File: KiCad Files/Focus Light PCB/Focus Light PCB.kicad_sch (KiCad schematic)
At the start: 1 part, among them SW1 TS1603-TZ38HBM

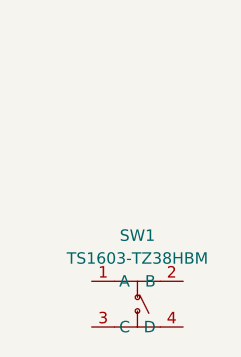
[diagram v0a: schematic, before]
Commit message: Small progress on kicad file due to switching over to easyeda
(KiCad folder will be deleted soon)
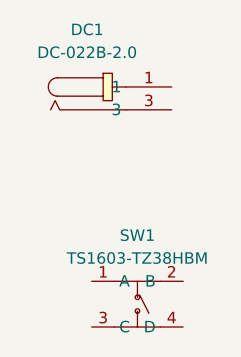
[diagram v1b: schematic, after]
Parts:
- added DC1: DC-022B-2.0, EasyEDA:DC-IN-TH_DC-022B-2.0, symbol EasyEDA:DC-022B-2.0
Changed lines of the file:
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@@
+		)
+	)
+	(symbol
+		(lib_id "EasyEDA:DC-022B-2.0")
+		(at 125.73 97.79 0)
+		(unit 1)
+		(body_style 1)
+		(exclude_from_sim no)
+		(in_bom yes)
+		(on_board yes)
+		(in_pos_files yes)
+		(dnp no)
+		(fields_autoplaced yes)
+		(property "Reference" "DC1"
+			(at 122.6822 91.44 0)
+			(show_name no)
+			(do_not_autoplace no)
+			(effects
+				(font
+					(size 1.27 1.27)
+				)
+			)
+		)
+		(property "Value" "DC-022B-2.0"
+			(at 122.6822 93.98 0)
+			(show_name no)
+			(do_not_autoplace no)
+			(effects
+				(font
+					(size 1.27 1.27)
+				)
+			)
+		)
+		(property "Footprint" "EasyEDA:DC-IN-TH_DC-022B-2.0"
+			(at 125.73 107.95 0)
+			(hide yes)
+			(show_name no)
+			(do_not_autoplace no)
+			(effects
+				(font
+					(size 1.27 1.27)
+				)
+			)
+		)
+		(property "Datasheet" "https://lcsc.com/product-detail/Power-Connectors_XKB-Enterprise-DC-022B-2-0_C319097.html"
+			(at 125.73 110.49 0)
+			(hide yes)
+			(show_name no)
+			(do_not_autoplace no)
+			(effects
+				(font
+					(size 1.27 1.27)
+				)
+			)
+		)
+		(property "Description" ""
+			(at 125.73 97.79 0)
+			(hide yes)
+			(show_name no)
+			(do_not_autoplace no)
+			(effects
+				(font
+					(size 1.27 1.27)
+				)
+			)
+		)
+		(property "Manufacturer" "XKB Connection(中国星坤)"
+			(at 125.73 113.03 0)
+			(hide yes)
+			(show_name no)
+			(do_not_autoplace no)
+			(effects
+				(font
+					(size 1.27 1.27)
+				)
+			)
+		)
+		(property "MPN" "DC-022B-2.0"
+			(at 125.73 115.57 0)
+			(hide yes)
+			(show_name no)
+			(do_not_autoplace no)
+			(effects
+				(font
+					(size 1.27 1.27)
+				)
+			)
+		)
+		(property "LCSC Part" "C319097"
+			(at 125.73 118.11 0)
+			(hide yes)
+			(show_name no)
+			(do_not_autoplace no)
+			(effects
+				(font
+					(size 1.27 1.27)
+				)
+			)
+		)
+		(pin "1"
+		)
+		(pin "3"
+		)
+		(instances
+			(project "Focus Light PCB"
+				(path "/283b5d99-c295-48e8-87cd-94914472b7a9"
+					(reference "DC1")
+					(unit 1)
+				)
+			)
 		)
 	)
